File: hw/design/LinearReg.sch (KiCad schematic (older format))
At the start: 7 parts

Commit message: updated libraries, new xfmr
updated libraries, selected transformer and added to library/documentation
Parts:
- removed U?: LT3086R, symbol RDSmith:LT3086R
- added U?: LT3086R, symbol pps_klib:LT3086R
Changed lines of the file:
@@
 	3100 4150 2950 4150
-$Comp
-L RDSmith:LT3086R U?
-U 1 1 5EB6D3E5
-P 6050 2450
-F 0 "U?" H 6050 3127 100 0000 C CNN
-F 1 "LT3086R" H 6050 2961 100 0000 C CNN
-F 2 "" H 6050 2450 100 0001 C CNN
-F 3 "" H 6050 2450 100 0001 C CNN
-	1    6050 2450
-	1    0    0    -1
-$EndComp
 $Comp
 L power:GND #PWR?
@@
 	1    0    0    -1
 $EndComp
+$Comp
+L pps_klib:LT3086R U?
+U 1 1 5EC5069B
+P 6050 2450
+F 0 "U?" H 6050 3127 100 0000 C CNN
+F 1 "LT3086R" H 6050 2961 100 0000 C CNN
+F 2 "" H 6050 2450 100 0001 C CNN
+F 3 "" H 6050 2450 100 0001 C CNN
+	1    6050 2450
+	1    0    0    -1
+$EndComp

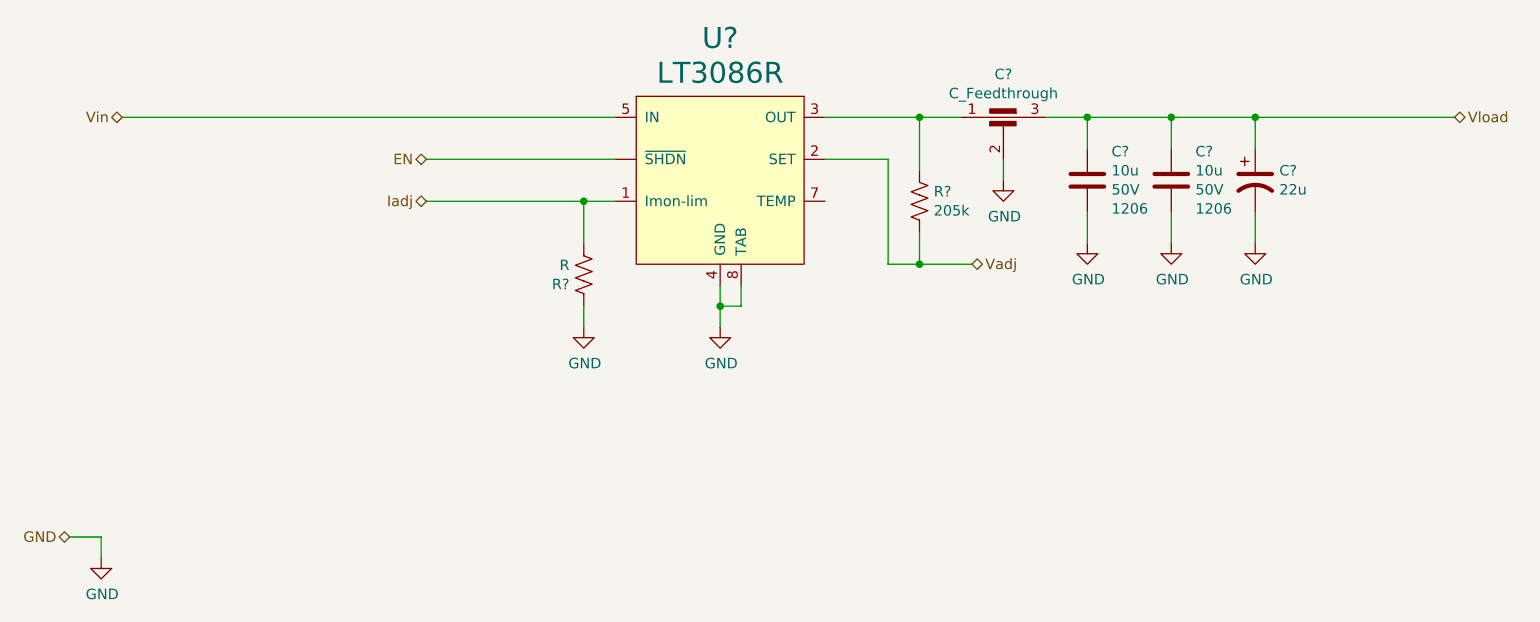
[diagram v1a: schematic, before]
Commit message: more work
more PFC work, more LDO work, added secondary regulator sheet, expanded system power tree sim
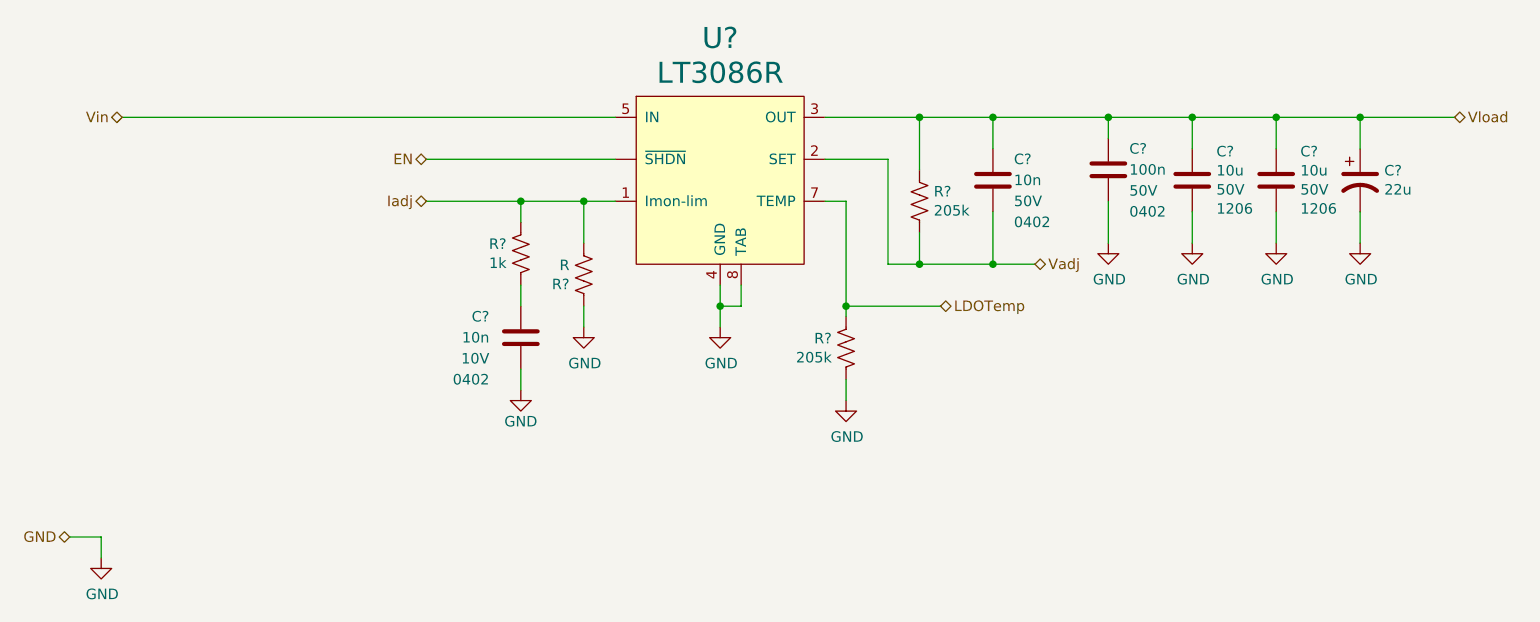
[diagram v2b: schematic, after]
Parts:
- removed C?: C_Feedthrough, symbol Device:C_Feedthrough
- added C?: 100n, Capacitor_SMD:C_0603_1608Metric, symbol Device:C
- added C? (x2): 10n, Capacitor_SMD:C_0603_1608Metric, symbol Device:C
- added R?: 205k, Resistor_SMD:R_0603_1608Metric, symbol Device:R_US
- added R?: 1k, Resistor_SMD:R_0603_1608Metric, symbol Device:R_US
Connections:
- net GND: now also C?.2, C?.2, R?.2
- net Iadj: now also R?.1
- net Vadj: now also C?.2
- net Vload: now also R?.1, U?.3 (OUT), C?.1, C?.1
- net LDOTemp: now reaches U?.7 (TEMP)
- net LDOTemp: now also R?.1
- new net: C?.1, R?.2
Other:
- moved on the sheet: C?

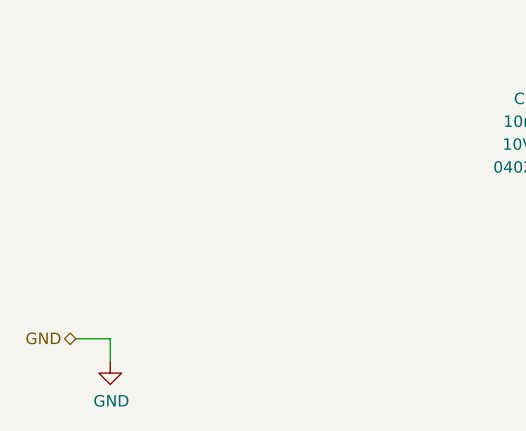
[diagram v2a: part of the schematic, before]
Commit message: lots of work
expanded README doc, specifications, added secondary regulator circuit + symbol, more component specs added
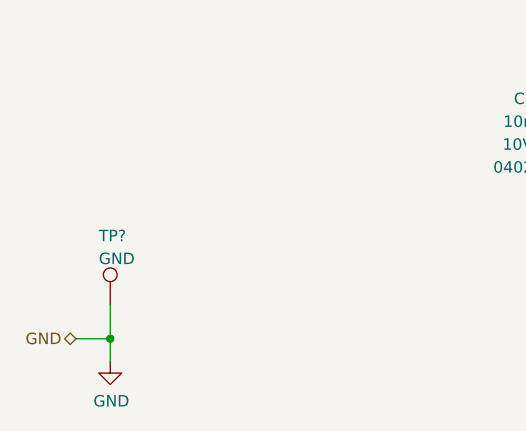
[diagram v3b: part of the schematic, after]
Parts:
- added TP?: GND, TestPoint:TestPoint_Keystone_5000-5004_Miniature, symbol Connector:TestPoint
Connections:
- net GND: now also TP?.1
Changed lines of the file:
@@
 Wire Wire Line
 	7350 2150 7900 2150
+$Comp
+L Connector:TestPoint TP?
+U 1 1 5ECDC050
+P 3100 4000
+AR Path="/5E80D1C0/5ECDC050" Ref="TP?"  Part="1"
+AR Path="/5E80D210/5ECDC050" Ref="TP?"  Part="1"
+AR Path="/5E84FADE/5ECDC050" Ref="TP?"  Part="1"
+AR Path="/5ECFB146/5ECDC050" Ref="TP?"  Part="1"
+AR Path="/5E917C1A/5ECDC050" Ref="TP?"  Part="1"
+F 0 "TP?" H 3050 4300 50  0000 L CNN
+F 1 "GND" H 3050 4200 50  0000 L CNN
+F 2 "TestPoint:TestPoint_Keystone_5000-5004_Miniature" H 3300 4000 50  0001 C CNN
+F 3 "~" H 3300 4000 50  0001 C CNN
+	1    3100 4000
+	1    0    0    -1
+$EndComp
+Wire Wire Line
+	3100 4000 3100 4150
+Connection ~ 3100 4150
 $EndSCHEMATC

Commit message: more part numbers
Added manfacturer part numbers to ICs, added descriptions to symbols in library
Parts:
- U?: MfrNum (none) -> ADI_LT3086ER
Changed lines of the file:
@@
 F 2 "" H 6050 2450 100 0001 C CNN
 F 3 "" H 6050 2450 100 0001 C CNN
+F 4 "ADI_LT3086ER" H 6050 2450 50  0001 C CNN "MfrNum"
 	1    6050 2450
 	1    0    0    -1
